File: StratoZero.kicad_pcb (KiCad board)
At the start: 2 copper layers, 65 x 30 mm, 37 parts, among them P1 GPS, P2 I2C, P3 BATT, P4 AN1, P5 1WIRE, P6 RPI-GPIO, Q1 2N7002, U1 LM2940, U2 RFM95HW, U3 MCP3002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

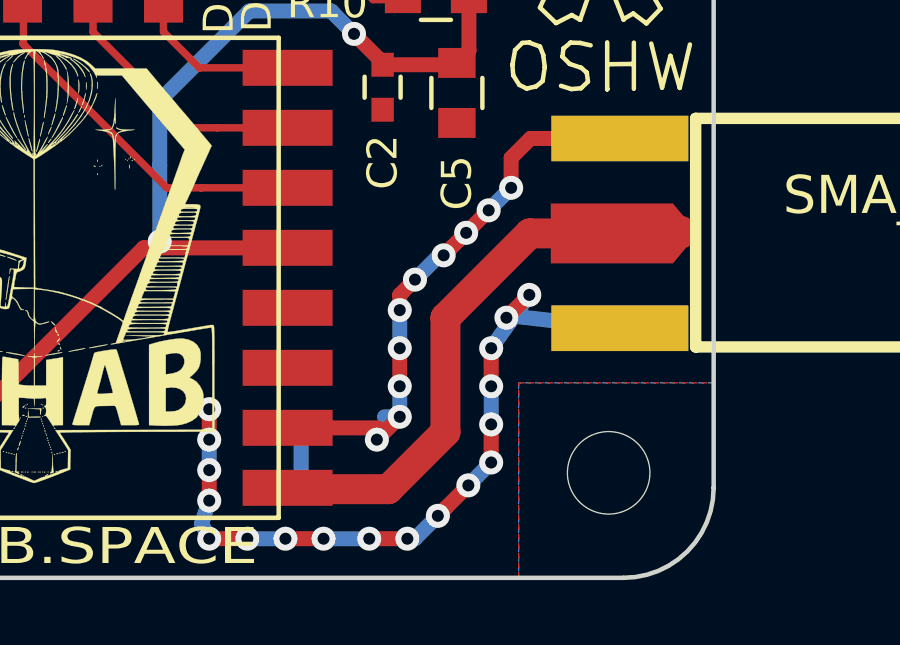
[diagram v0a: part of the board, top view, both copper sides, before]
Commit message: Improved RF Path
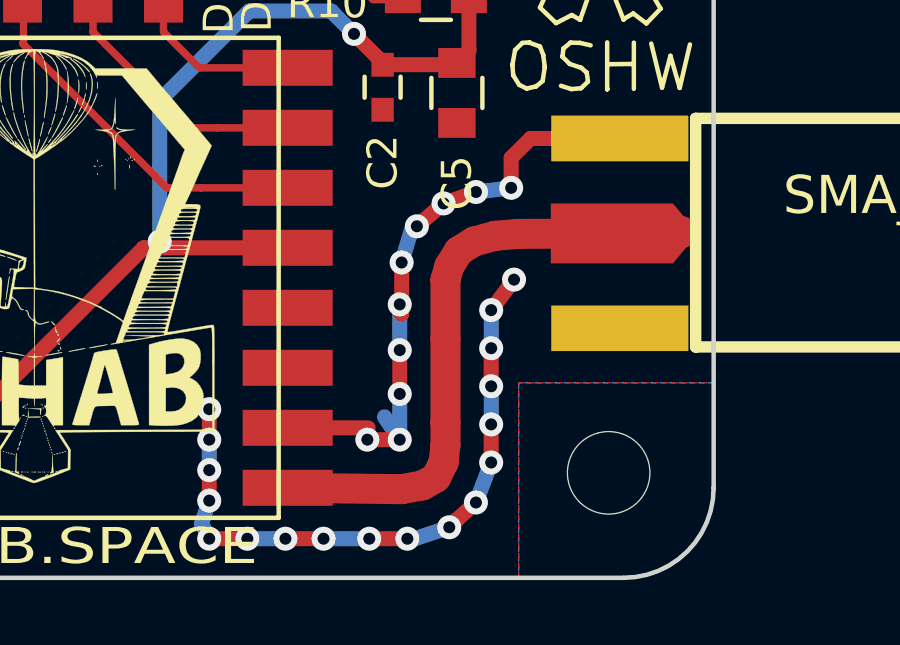
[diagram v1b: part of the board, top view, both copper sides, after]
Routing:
- net GND: track 57.8 -> 34.8 mm, vias 34 -> 16
- net (no net): track 1.25 -> 21.8 mm, vias 0 -> 18
- net /RF: track 18.9 -> 20.3 mm

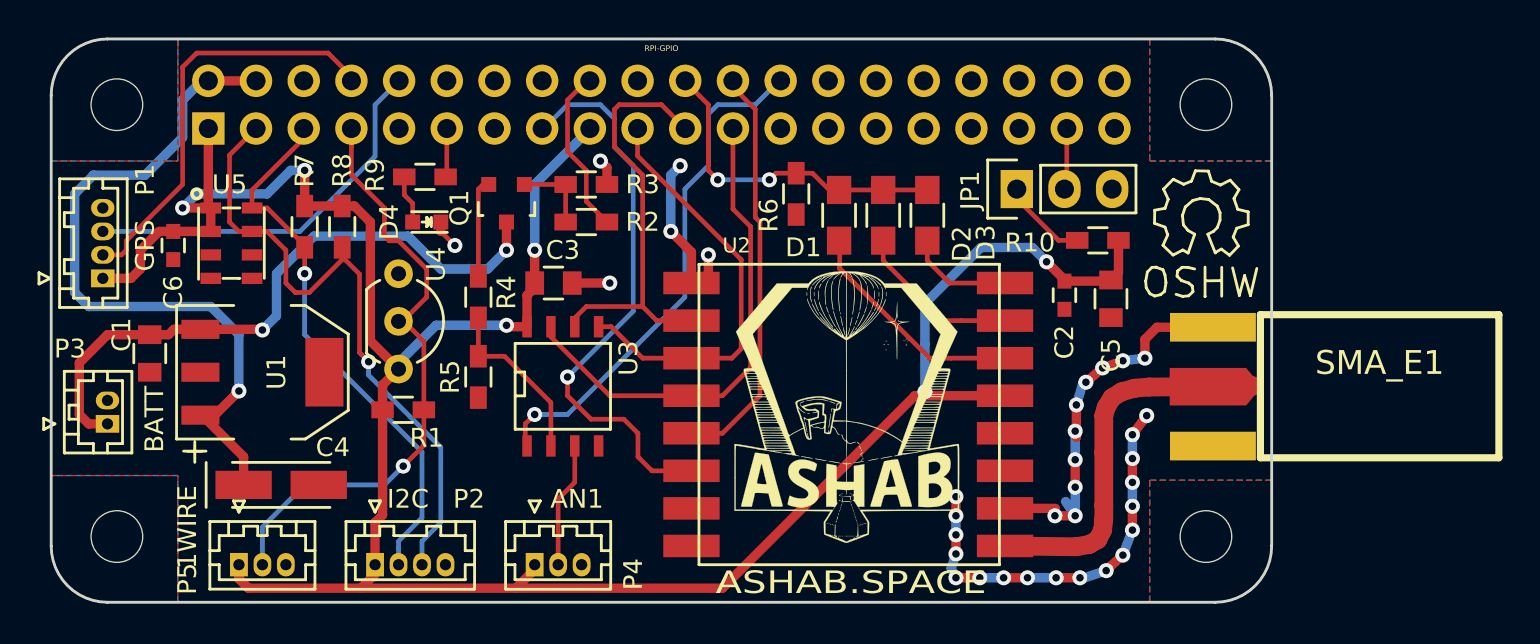
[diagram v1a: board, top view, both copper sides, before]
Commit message: Updated to V4, minor fixes and new RTC and battery on board
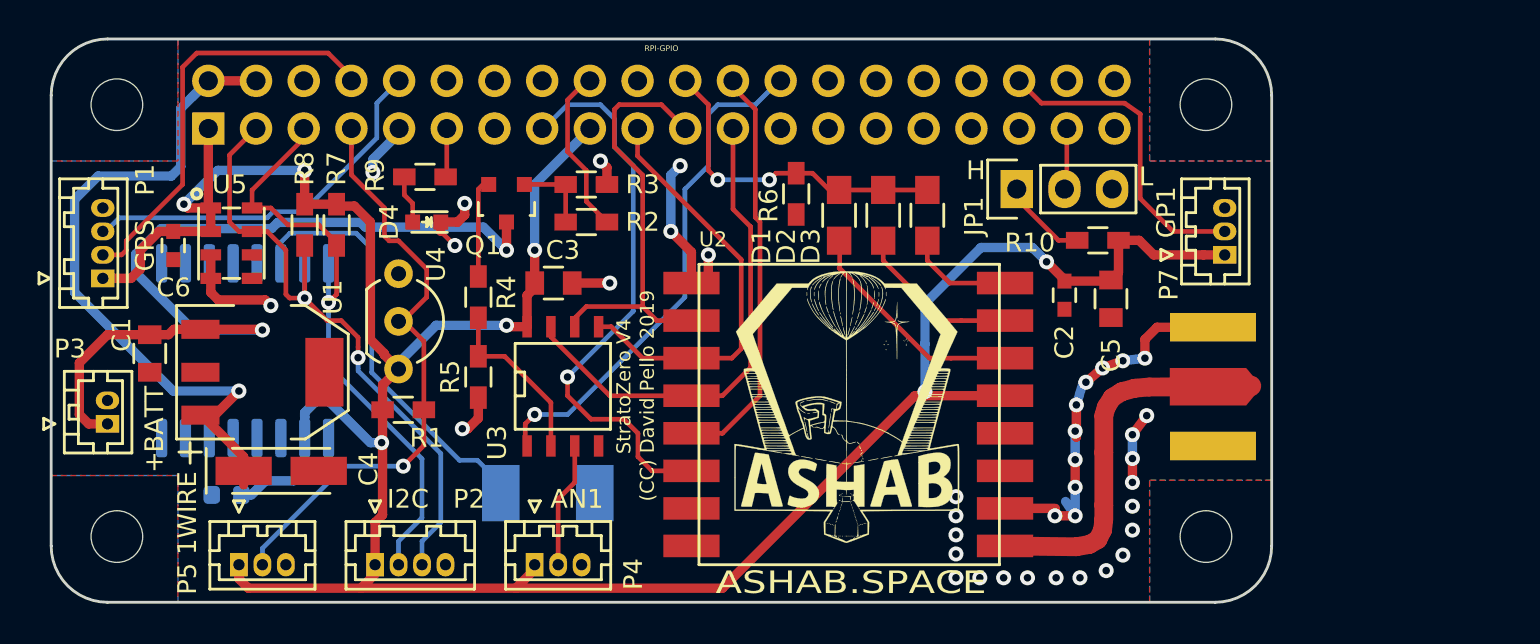
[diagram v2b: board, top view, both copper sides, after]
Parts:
- added BT1: Battery_Cell, ladecadence:RTC-Batt, B.Cu at (132.9, 96.2)
- added C7: 100n, Capacitor_SMD:C_0603_1608Metric, B.Cu at (115.8, 103.3)
- added G***: LOGO, Banana:Banana, F.Cu at (165.3, 108.2)
- added P7: GP1, Connectors_Hirose:Hirose_DF13-03P-1.25DSA_03x1.25mm_Straight, F.Cu at (169.0, 90.5)
- added U6: DS3231M, Package_SO:SOIC-16W_7.5x10.3mm_P1.27mm, B.Cu at (116.8, 95.6)
- ?: moved to B.Cu
- moved ? 5.90 mm to (162.5, 91.2), turned to 180 degrees
- moved R8 2.00 mm to (120.0, 88.9)
- moved R7 1.70 mm to (121.7, 88.9)
- moved C4 0.75 mm to (118.8, 102.0)
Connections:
- P6 pad 36: Net-(P6-Pad36) -> EXT_GPIO
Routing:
- net VMEM: track 0.00 -> 22.9 mm
- net (no net): track 21.8 -> 0.00 mm, vias 18 -> 0
- net +3V3: track 135.7 -> 153.4 mm, vias 6 -> 7
- net EXT_GPIO: track 0.00 -> 16.9 mm
- net GND: track 34.8 -> 51.3 mm, vias 16 -> 38
- net +BATT: track 34.0 -> 46.5 mm
- net SCL: track 29.1 -> 32.6 mm
- net SDA: track 34.5 -> 35.4 mm, vias 1 -> 2
- net 1WIRE: track 32.7 -> 32.1 mm
- net RXD: track 20.7 -> 20.2 mm
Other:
- board text added: "(CC) David Pello 2019"
- board text added: "David Pello 2019"
- board text added: "H"
- board text added: "L"
- board text added: "StratoZero V4"
- board text removed: "David Pello 2016"
